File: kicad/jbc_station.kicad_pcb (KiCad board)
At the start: 2 copper layers, 125 x 125 mm, 276 parts, among them J1 PWR, J15 Conn_01x07, J2 Conn_01x02, J21 Conn_01x07, J3 Barcode, J4 Front panel, J5 Conn_01x03, J6 Conn_01x05, J7 Conn_01x04, J8 Conn_01x03, J9 Conn_01x07, Q1 BSS138, Q2 BSS138, Q3 BSS138, Q4 AON6448, Q5 AON6448, Q6 AON6448, Q7 AON6448, Q8 AON6448, Q9 AON6448, U1 L78L05_SOT89, U10 CH9141K, U11 LM5106MM, U12 AD8221ARMZ, U13 LM5106MM, U14 AD8221ARMZ, U15 LM5106MM, U16 AD8221ARMZ, U17 XC6206PxxxMR, U2 LP2985-3.3, U3 ICL7660, U4 HT7463, U5 HT7463, U6 XC6206PxxxMR, U7 M24C64, U8 INA3221, U9 STM32F401CCUx, Y1 Crystal, Y2 Crystal

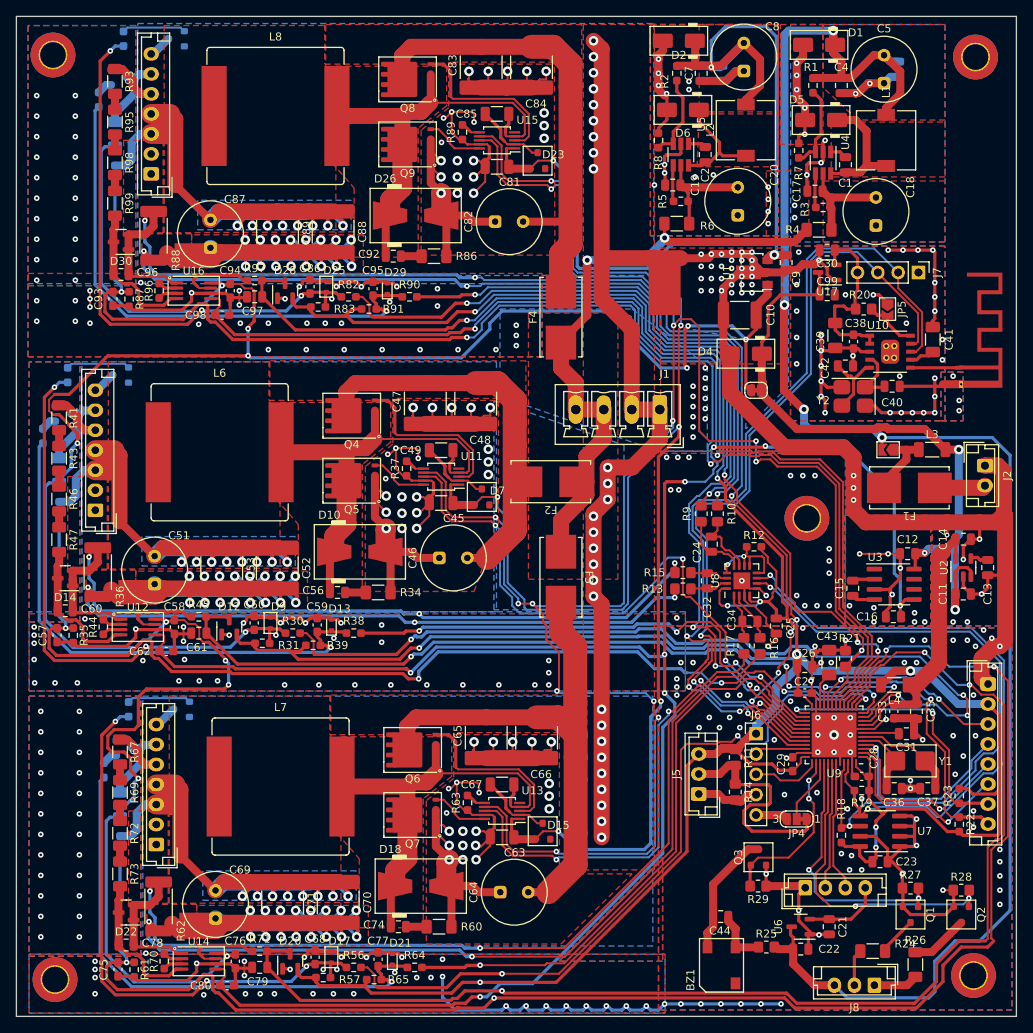
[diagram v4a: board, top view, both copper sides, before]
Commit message: Add more filtering caps for ADC
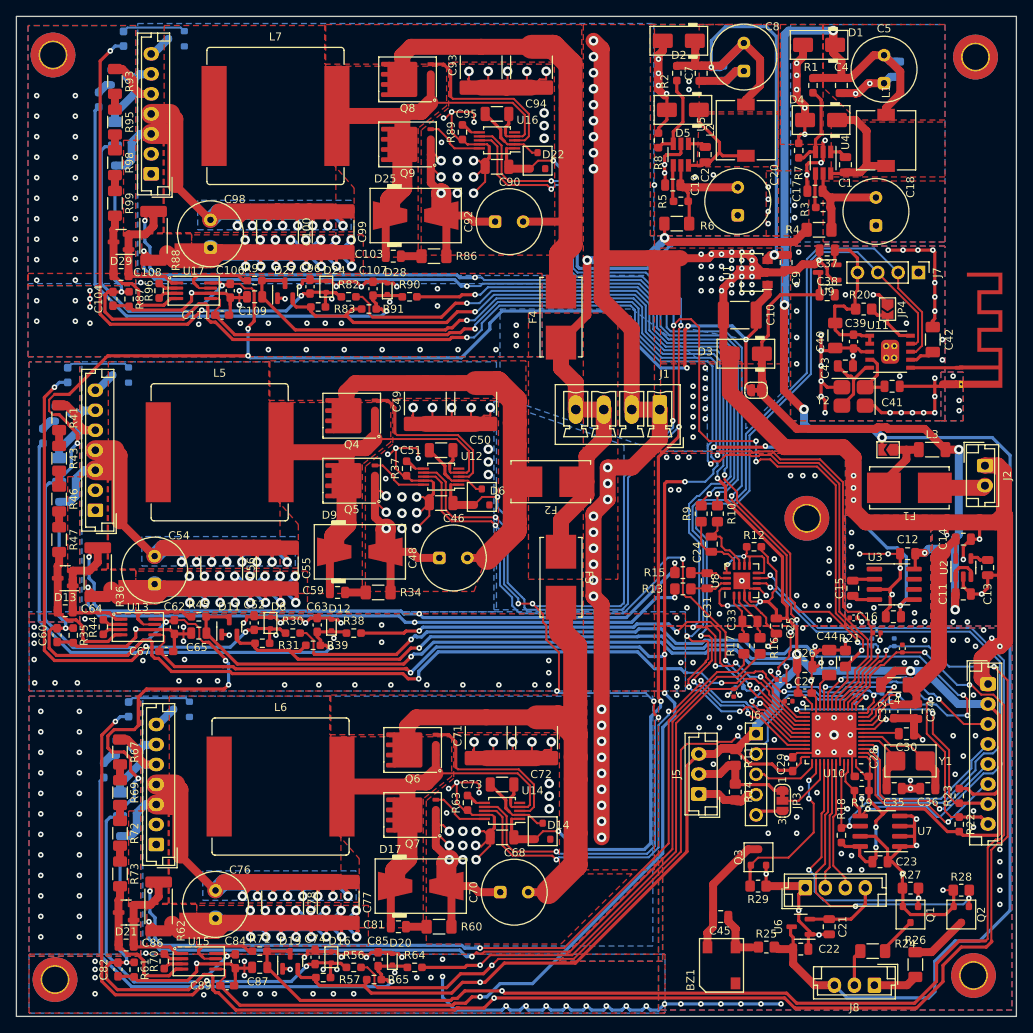
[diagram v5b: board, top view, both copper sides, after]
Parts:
- added C105: 10n, Capacitor_SMD:C_0402_1005Metric, B.Cu at (90.4, 83.9)
- added C110: 10n, Capacitor_SMD:C_0402_1005Metric, F.Cu at (107.5, 77.1)
- added C47: 10n, Capacitor_SMD:C_0402_1005Metric, B.Cu at (109.2, 85.1)
- added C53: 10n, Capacitor_SMD:C_0402_1005Metric, B.Cu at (108.2, 85.1)
- added C61: 10n, Capacitor_SMD:C_0402_1005Metric, F.Cu at (96.5, 85.6)
- added C66: 10n, Capacitor_SMD:C_0402_1005Metric, F.Cu at (95.5, 82.9)
- added C69: 10n, Capacitor_SMD:C_0402_1005Metric, B.Cu at (104.9, 85.3)
- added C75: 10n, Capacitor_SMD:C_0402_1005Metric, B.Cu at (109.7, 78.2)
- added C83: 10n, Capacitor_SMD:C_0402_1005Metric, F.Cu at (89.7, 84.6)
- added C88: 10n, Capacitor_SMD:C_0402_1005Metric, F.Cu at (110.7, 79.0)
- added C91: 10n, Capacitor_SMD:C_0402_1005Metric, B.Cu at (106.9, 78.3)
- added C97: 10n, Capacitor_SMD:C_0402_1005Metric, F.Cu at (104.6, 75.2)
- moved JP3 2.89 mm to (95.8, 98.0), turned to -90 degrees
- renumbered C89 to C100, C90 to C101, C91 to C102, C92 to C103, C93 to C104, C94 to C106, C95 to C107, C96 to C108, C97 to C109, C98 to C111, C31 to C30, C32 to C31, C33 to C32, C34 to C33, C35 to C34, C36 to C35, C37 to C36, C30 to C37, C99 to C38, C38 to C39, C39 to C40, C40 to C41, C41 to C42, C42 to C43, C43 to C44, C44 to C45, C45 to C46, C46 to C48, C47 to C49, C48 to C50, C49 to C51, C50 to C52, C51 to C54, C52 to C55, C53 to C56, C54 to C57, C55 to C58, C56 to C59, C57 to C60, C58 to C62, C59 to C63, C60 to C64, C61 to C65, C62 to C67, C63 to C68, C64 to C70, C65 to C71, C66 to C72, C67 to C73, C68 to C74, C69 to C76, C70 to C77, C71 to C78, C72 to C79, C73 to C80, C74 to C81, C75 to C82, C76 to C84, C77 to C85, C78 to C86, C79 to C87, C80 to C89, C81 to C90, C82 to C92, C83 to C93, C84 to C94, C85 to C95, C86 to C96, C87 to C98, C88 to C99, D11 to D10, D12 to D11, D13 to D12, D14 to D13, D15 to D14, D16 to D15, D17 to D16, D18 to D17, D19 to D18, D20 to D19, D21 to D20, D22 to D21, D23 to D22, D24 to D23, D25 to D24, D26 to D25, D27 to D26, D28 to D27, D29 to D28, D30 to D29, D4 to D3, D5 to D4, D6 to D5, D7 to D6, D8 to D7, D9 to D8, D10 to D9, JP4 to JP3, JP5 to JP4, L6 to L5, L7 to L6, L8 to L7, NT4 to NT2, NT5 to NT3, NT6 to NT4, U9 to U10, U10 to U11, U11 to U12, U12 to U13, U13 to U14, U14 to U15, U15 to U16, U16 to U17, U17 to U9
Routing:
- net /POWER_SW: track 29.0 -> 13.7 mm
- net GND: track 515.9 -> 520.4 mm, vias 347 -> 361
- net -5V: track 322.7 -> 324.0 mm
- net /V_{OUT}1: track 136.1 -> 137.4 mm
- net /HNDL_{SEN}1: track 109.7 -> 110.8 mm
- net /TC_{OUT}3: track 131.7 -> 132.5 mm
- net /PWM_{EN}: track 259.4 -> 258.8 mm
- added copper zone on F.Cu, net Net-(D10-K)
- added copper zone on F.Cu, net Net-(D18-K)
- added copper zone on F.Cu, net Net-(D26-K)
- added copper zone on F.Cu, net Net-(D6-K)
- removed copper zone on F.Cu, net Net-(D17-K)
- removed copper zone on F.Cu, net Net-(D25-K)
- removed copper zone on F.Cu, net Net-(D4-K)
- removed copper zone on F.Cu, net Net-(D9-K)
